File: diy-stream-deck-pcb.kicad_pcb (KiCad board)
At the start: 2 copper layers, 40 parts, among them J1 USB_C_Receptacle_USB2.0_16P, SW1 BOOT, SW2 RESET, SW3 CMD1, SW4 CMD2, SW5 CMD3, SW6 CMD4, U1 USBLC6-2SC6, U2 AP2112K-3.3, U3 ESP32-C3-WROOM-02

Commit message: Feat: added pinout for GPIO
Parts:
- added J2: Conn_01x06_Pin, Connector_PinHeader_2.54mm:PinHeader_1x06_P2.54mm_Vertical, F.Cu at (126.2, 25.5)
- moved R16 50.9 mm to (118.7, 55.5), turned to 180 degrees
- moved R15 34.0 mm to (94.4, 55.5)
- moved D4 30.0 mm to (101.0, 25.0)
- moved D3 27.0 mm to (108.5, 25.0)
- moved R17 26.6 mm to (94.4, 60.5)
- moved D2 9.73 mm to (93.5, 25.0)
- moved U1 5.02 mm to (126.5, 30.5)
- moved C10 2.50 mm to (115.0, 49.5)
- moved R14 1.54 mm to (111.5, 43.5)
- moved J1 1.35 mm to (136.8, 23.1)
- moved R13 1.06 mm to (111.5, 39.0)
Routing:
- net GND: track 0.00 -> 1.37 mm

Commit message: Feat: initial pcb layout
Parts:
- moved R17 40.6 mm to (101.6, 20.5), turned to 180 degrees
- moved R15 40.4 mm to (114.6, 20.5), turned to 180 degrees
- moved R16 36.5 mm to (129.2, 20.5)
- moved R7 13.2 mm to (131.4, 38.0), turned to 0 degrees
- moved R4 12.8 mm to (137.9, 30.5)
- moved U2 12.5 mm to (148.6, 23.0)
- moved R2 10.6 mm to (130.8, 24.0)
- moved D2 7.56 mm to (101.0, 25.5)
- moved D4 7.06 mm to (94.0, 25.5)
- moved R1 6.38 mm to (130.8, 26.5)
- moved C5 4.72 mm to (146.1, 35.5), turned to 180 degrees
- moved C7 4.40 mm to (153.9, 53.0)
- moved R6 4.12 mm to (146.0, 39.0), turned to 180 degrees
- moved R8 4.12 mm to (149.9, 45.5), turned to 180 degrees
- moved C6 4.00 mm to (154.0, 57.0)
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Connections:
- J2 pad 1: IO1 -> unconnected-(J2-Pin_1-Pad1)
- J2 pad 2: IO2 -> unconnected-(J2-Pin_2-Pad2)
- J2 pad 3: IO3 -> IO10
- J2 pad 4: IO4 -> IO3
- J2 pad 5: IO8 -> IO2
- J2 pad 6: IO10 -> IO1
- R17 pad 1: IO7 -> +3V3
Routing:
- net +3V3: track 0.00 -> 227.1 mm
- net IO0: track 0.00 -> 85.1 mm
- net IO5: track 0.00 -> 75.7 mm
- net IO6: track 0.00 -> 59.8 mm
- net IO2: track 0.00 -> 49.6 mm
- net IO1: track 0.00 -> 39.1 mm
- net Net-(R12-Pad2): track 0.00 -> 31.9 mm
- net IO3: track 0.00 -> 31.1 mm
- net EN: track 0.00 -> 23.9 mm
- net USB_D+: track 0.00 -> 22.8 mm
- net Net-(R11-Pad2): track 0.00 -> 22.3 mm
- net IO10: track 0.00 -> 21.0 mm
- net Net-(D3-A): track 0.00 -> 20.4 mm
- net VBUS: track 0.00 -> 18.7 mm
- net USB_D-: track 0.00 -> 18.7 mm
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
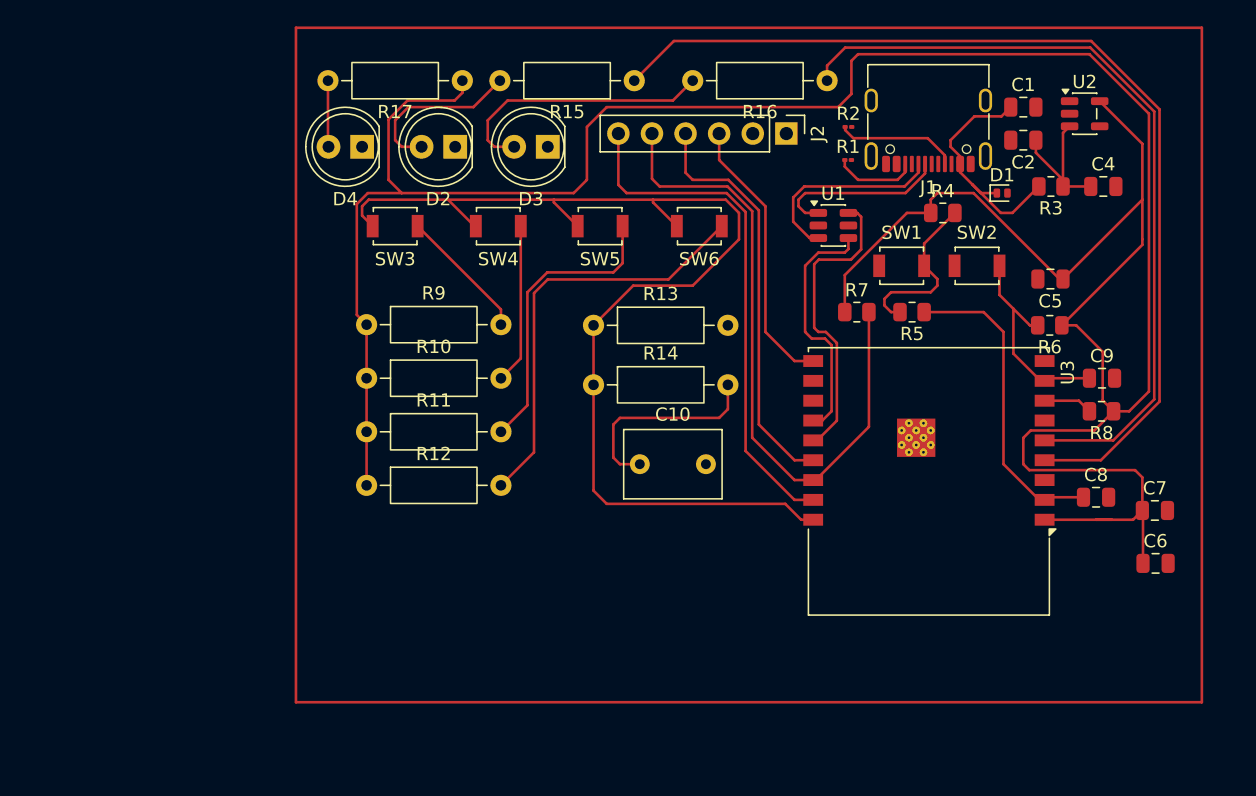
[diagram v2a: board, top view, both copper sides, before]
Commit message: Fix: usb footprint for 0.2mm copper-hole tolerance. DRC layout errors
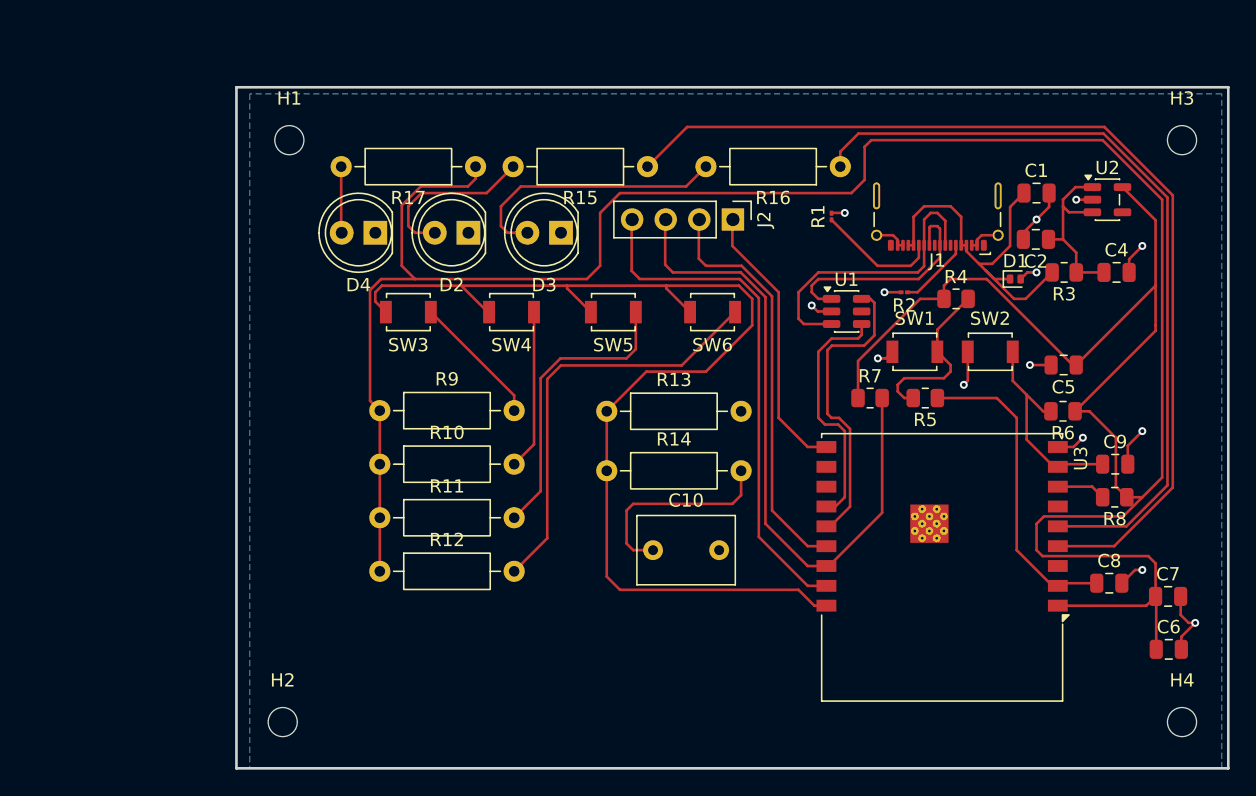
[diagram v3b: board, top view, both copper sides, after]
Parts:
- added H1: MountingHole, MountingHole:MountingHole_2.2mm_M2, F.Cu at (88.5, 25.0)
- added H2: MountingHole, MountingHole:MountingHole_2.2mm_M2, F.Cu at (88.0, 69.0)
- added H3: MountingHole, MountingHole:MountingHole_2.2mm_M2, F.Cu at (156.0, 25.0)
- added H4: MountingHole, MountingHole:MountingHole_2.2mm_M2, F.Cu at (156.0, 69.0)
- J1: footprint Connector_USB:USB_C_Receptacle_G-Switch_GT-USB-7010ASV -> Connector_USB:USB_C_Receptacle_G-Switch_GT-USB-7025
- J2: value Conn_01x06_Pin -> Conn_01x04_Pin; footprint Connector_PinHeader_2.54mm:PinHeader_1x06_P2.54mm_Vertical -> Connector_PinHeader_2.54mm:PinHeader_1x04_P2.54mm_Vertical
- moved R2 13.2 mm to (135.0, 36.5), turned to 180 degrees
- moved J2 7.65 mm to (122.0, 31.0)
- moved C2 7.56 mm to (144.9, 32.5)
- moved U2 6.73 mm to (150.4, 29.5)
- moved U1 6.58 mm to (130.6, 38.0)
- moved C1 6.58 mm to (145.0, 29.0)
- moved C10 6.58 mm to (116.0, 56.0)
- moved C4 6.58 mm to (151.1, 35.0)
- moved C5 6.58 mm to (147.1, 42.0)
- moved C6 6.58 mm to (155.0, 63.5)
- moved C7 6.58 mm to (154.9, 59.5)
- moved C8 6.58 mm to (150.5, 58.5)
- moved C9 6.58 mm to (150.9, 49.5)
- moved D1 6.58 mm to (143.4, 35.5)
- moved D2 6.58 mm to (102.0, 32.0)
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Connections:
- J2 pad 1: unconnected-(J2-Pin_1-Pad1) -> IO10
- J2 pad 2: unconnected-(J2-Pin_2-Pad2) -> IO3
- J2 pad 3: IO10 -> IO2
- J2 pad 4: IO3 -> IO1
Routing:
- net GND: track 0.00 -> 37.3 mm, vias 0 -> 14
- net VBUS: track 18.7 -> 28.1 mm
- net /D-: track 15.1 -> 22.4 mm
- net /D+: track 13.3 -> 17.2 mm
- net Net-(J1-CC1): track 9.22 -> 5.50 mm
- net +5V: track 11.3 -> 14.2 mm
- net Net-(J1-CC2): track 6.34 -> 9.23 mm
- added copper zone on B.Cu, net GND
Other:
- board outline added: 75 x 51.5 mm

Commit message: Fix: DRC errors layout
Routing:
- net +3V3: track 226.8 -> 228.1 mm
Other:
- board text added: "BOOT"
- board text added: "RESET"

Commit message: Fix text labels
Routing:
- net Net-(R12-Pad2): track 31.9 -> 35.1 mm
- net IO0: track 85.1 -> 86.2 mm
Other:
- board text added: "CMD1"
- board text added: "CMD2"
- board text added: "CMD3"
- board text added: "CMD4"
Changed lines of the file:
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@@
 		(capping no)
 		(filling no)
+		(zone_defaults)
 		(pcbplotparams
 			(layerselection 0x00000000_00000000_55555555_5755f5ff)
@@
 			(at 0 -2.5 0)
 			(layer "F.SilkS")
+			(hide yes)
 			(effects
 				(font
@@
 			(at 0 -2.5 0)
 			(layer "F.SilkS")
+			(hide yes)
 			(effects
 				(font
@@
 			(at 0 -2.5 0)
 			(layer "F.SilkS")
+			(hide yes)
 			(effects
 				(font
@@
 			(at 0 -2.5 0)
 			(layer "F.SilkS")
+			(hide yes)
 			(effects
 				(font
@@
 		(layer "Edge.Cuts")
 	)
+	(gr_text "CMD1"
+		(at 95 41 0)
+		(layer "F.SilkS")
+		(effects
+			(font
+				(size 1 1)
+				(thickness 0.15)
+			)
+			(justify left bottom)
+		)
+	)
+	(gr_text "CMD2"
+		(at 103.28087 41.024382 0)
+		(layer "F.SilkS")
+		(effects
+			(font
+				(size 1 1)
+				(thickness 0.15)
+			)
+			(justify left bottom)
+		)
+	)
+	(gr_text "CMD3"
+		(at 110.5 41 0)
+		(layer "F.SilkS")
+		(effects
+			(font
+				(size 1 1)
+				(thickness 0.15)
+			)
+			(justify left bottom)
+		)
+	)
+	(gr_text "CMD4"
+		(at 118.5 41 0)
+		(layer "F.SilkS")
+		(effects
+			(font
+				(size 1 1)
+				(thickness 0.15)
+			)
+			(justify left bottom)
+		)
+	)
 	(gr_text "BOOT\n"
 		(at 133.5 39.3 0)
@@
 	)
 	(segment
-		(start 123.5 37)
-		(end 123.5 39)
+		(start 101.5 36)
+		(end 109.5 36)
 		(width 0.2)
 		(layer "F.Cu")
@@
 	)
 	(segment
-		(start 101.5 36)
-		(end 109.5 36)
+		(start 123.5 40.924264)
+		(end 123.5 37)
 		(width 0.2)
 		(layer "F.Cu")
@@
 	)
 	(segment
-		(start 115.5 42.5)
-		(end 112.5 45.5)
+		(start 112.5 45.5)
+		(end 115.5 42.5)
+		(width 0.2)
+		(layer "F.Cu")
+		(net "IO0")
+	)
+	(segment
+		(start 122.5 36)
+		(end 117 36)
 		(width 0.2)
 		(layer "F.Cu")
@@
 	)
 	(segment
-		(start 122.5 36)
-		(end 123.5 37)
-		(width 0.2)
-		(layer "F.Cu")
-		(net "IO0")
-	)
-	(segment
 		(start 95 37.2)
 		(end 95 36.5)
@@
 	)
 	(segment
-		(start 109.5 36)
-		(end 117 36)
+		(start 115.5 42.5)
+		(end 121.924264 42.5)
 		(width 0.2)
 		(layer "F.Cu")
@@
 	)
 	(segment
-		(start 117 36)
-		(end 122.5 36)
+		(start 109.5 36)
+		(end 117 36)
 		(width 0.2)
 		(layer "F.Cu")
@@
 	)
 	(segment
-		(start 127 59)
-		(end 128.2 60.2)
+		(start 121.924264 42.5)
+		(end 123.5 40.924264)
 		(width 0.2)
 		(layer "F.Cu")
@@
 	)
 	(segment
-		(start 109.5 36.2)
-		(end 109.5 36)
+		(start 127 59)
+		(end 128.2 60.2)
 		(width 0.2)
 		(layer "F.Cu")
@@
 	)
 	(segment
-		(start 95.8 38)
-		(end 95 37.2)
+		(start 123.5 37)
+		(end 122.5 36)
 		(width 0.2)
 		(layer "F.Cu")
@@
 	)
 	(segment
-		(start 128.2 60.2)
-		(end 129.11 60.2)
+		(start 109.5 36.2)
+		(end 109.5 36)
 		(width 0.2)
 		(layer "F.Cu")
@@
 	)
 	(segment
-		(start 123.5 39)
-		(end 120 42.5)
+		(start 95.8 38)
+		(end 95 37.2)
 		(width 0.2)
 		(layer "F.Cu")
@@
 	)
 	(segment
-		(start 113.5 59)
-		(end 127 59)
+		(start 128.2 60.2)
+		(end 129.11 60.2)
 		(width 0.2)
 		(layer "F.Cu")
@@
 	)
 	(segment
-		(start 120 42.5)
-		(end 115.5 42.5)
+		(start 113.5 59)
+		(end 127 59)
 		(width 0.2)
 		(layer "F.Cu")
@@
 	)
 	(segment
-		(start 108 43.065686)
-		(end 109.032843 42.032843)
+		(start 121.967157 42.032843)
+		(end 123.2 40.8)
 		(width 0.2)
 		(layer "F.Cu")
@@
 	)
 	(segment
-		(start 105.5 57.6)
-		(end 108 55.1)
+		(start 123.2 40.8)
+		(end 123.2 38.7)
 		(width 0.2)
 		(layer "F.Cu")
@@
 	)
 	(segment
-		(start 118.167157 42.032843)
+		(start 122.5 38)
 		(end 122.2 38)
 		(width 0.2)
@@
 	)
 	(segment
+		(start 108 43.065686)
+		(end 109.032843 42.032843)
+		(width 0.2)
+		(layer "F.Cu")
+		(net "Net-(R12-Pad2)")
+	)
+	(segment
+		(start 105.5 57.6)
+		(end 108 55.1)
+		(width 0.2)
+		(layer "F.Cu")
+		(net "Net-(R12-Pad2)")
+	)
+	(segment
 		(start 109.032843 42.032843)
-		(end 118.167157 42.032843)
+		(end 121.967157 42.032843)
+		(width 0.2)
+		(layer "F.Cu")
+		(net "Net-(R12-Pad2)")
+	)
+	(segment
+		(start 123.2 38.7)
+		(end 122.5 38)
 		(width 0.2)
 		(layer "F.Cu")

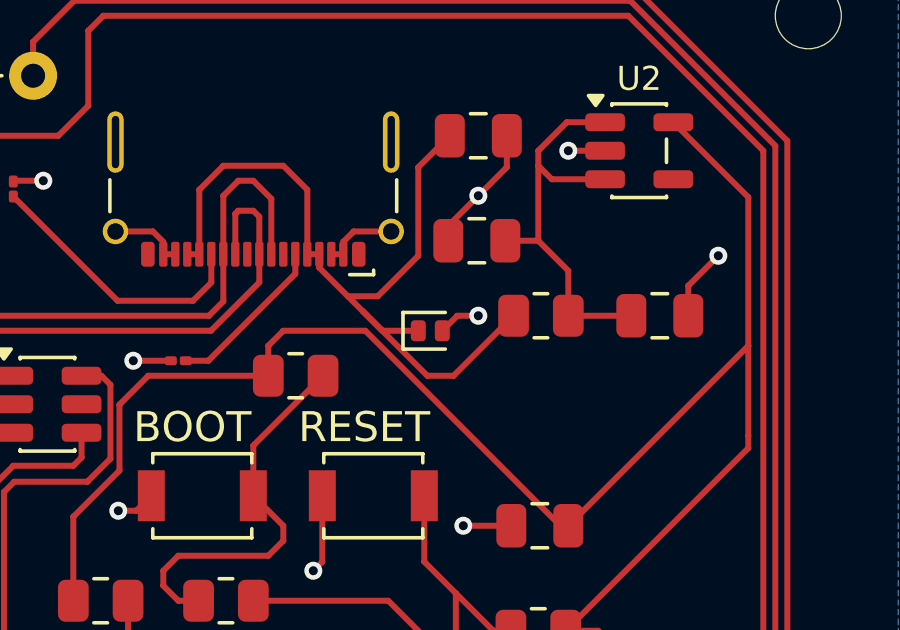
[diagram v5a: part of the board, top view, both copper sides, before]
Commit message: Fix useless components
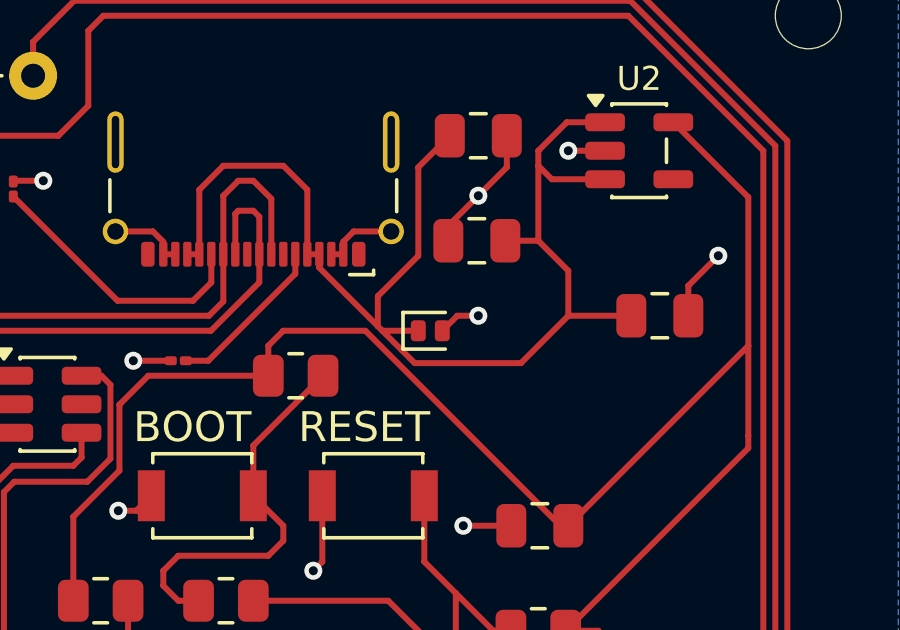
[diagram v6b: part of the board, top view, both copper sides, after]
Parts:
- removed R3: 0, Resistor_SMD:R_0805_2012Metric
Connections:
- C1 pad 1: VBUS -> +5V
- D1 pad 1: VBUS -> +5V
- J1 pad A4: VBUS -> +5V
- J1 pad A9: VBUS -> +5V
- J1 pad B4: VBUS -> +5V
- J1 pad B9: VBUS -> +5V
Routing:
- net +5V: track 14.2 -> 42.8 mm
- net VBUS: track 28.1 -> 0.00 mm
